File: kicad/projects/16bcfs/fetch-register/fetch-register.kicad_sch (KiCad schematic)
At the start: 104 parts, among them J1 InstrRegInput, J2 ALU Bus B, J3 FetchBusInput, J4 Main Bus, J5 Control Signals, J6 Address Bus 2, J7 Power, U1 74HC574, U10 74HC574, U11 74HC574, U12 74HC541, U2 74HC574, U3 74HC574, U4 74HC574, U5 74HC574, U6 74HC574, U7 74HC04, U8 74HC574, U9 74HC574

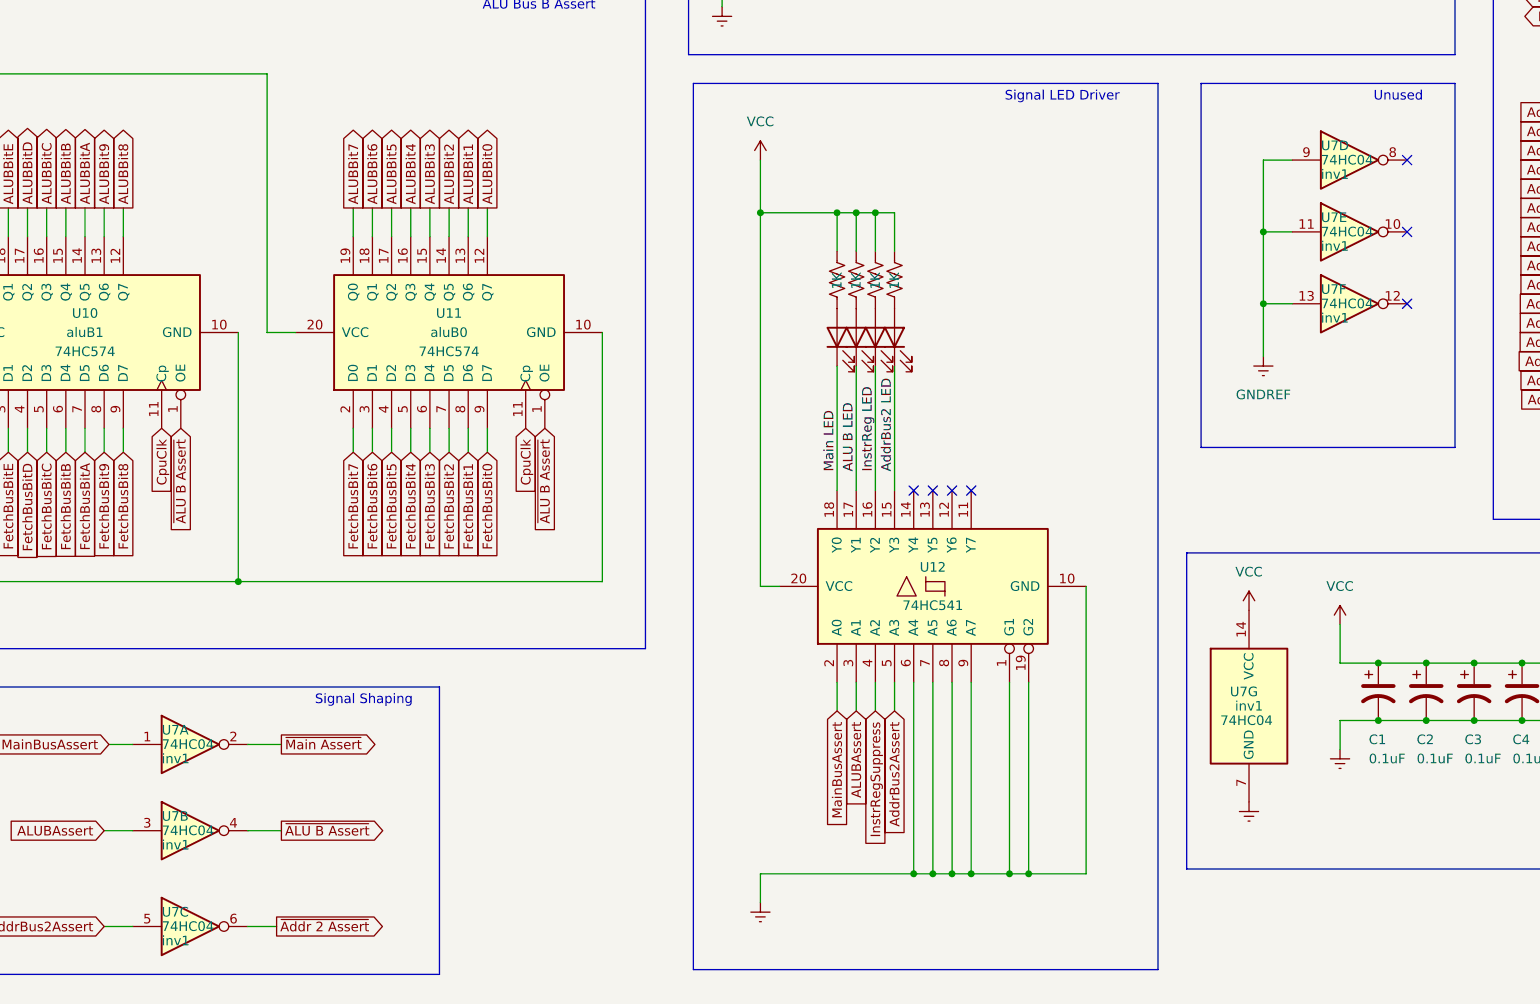
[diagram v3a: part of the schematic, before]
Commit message: Complete Component Placement on the Fetch Reg PCB
This commit handles all the component placement on the PCB for the Fetch
Register ahead of routing traces.  The expectation is that there is
plenty of room for traces.

Nothing has been done for 0R Resistors or test points yet.  Those will
be added ahead of routing.
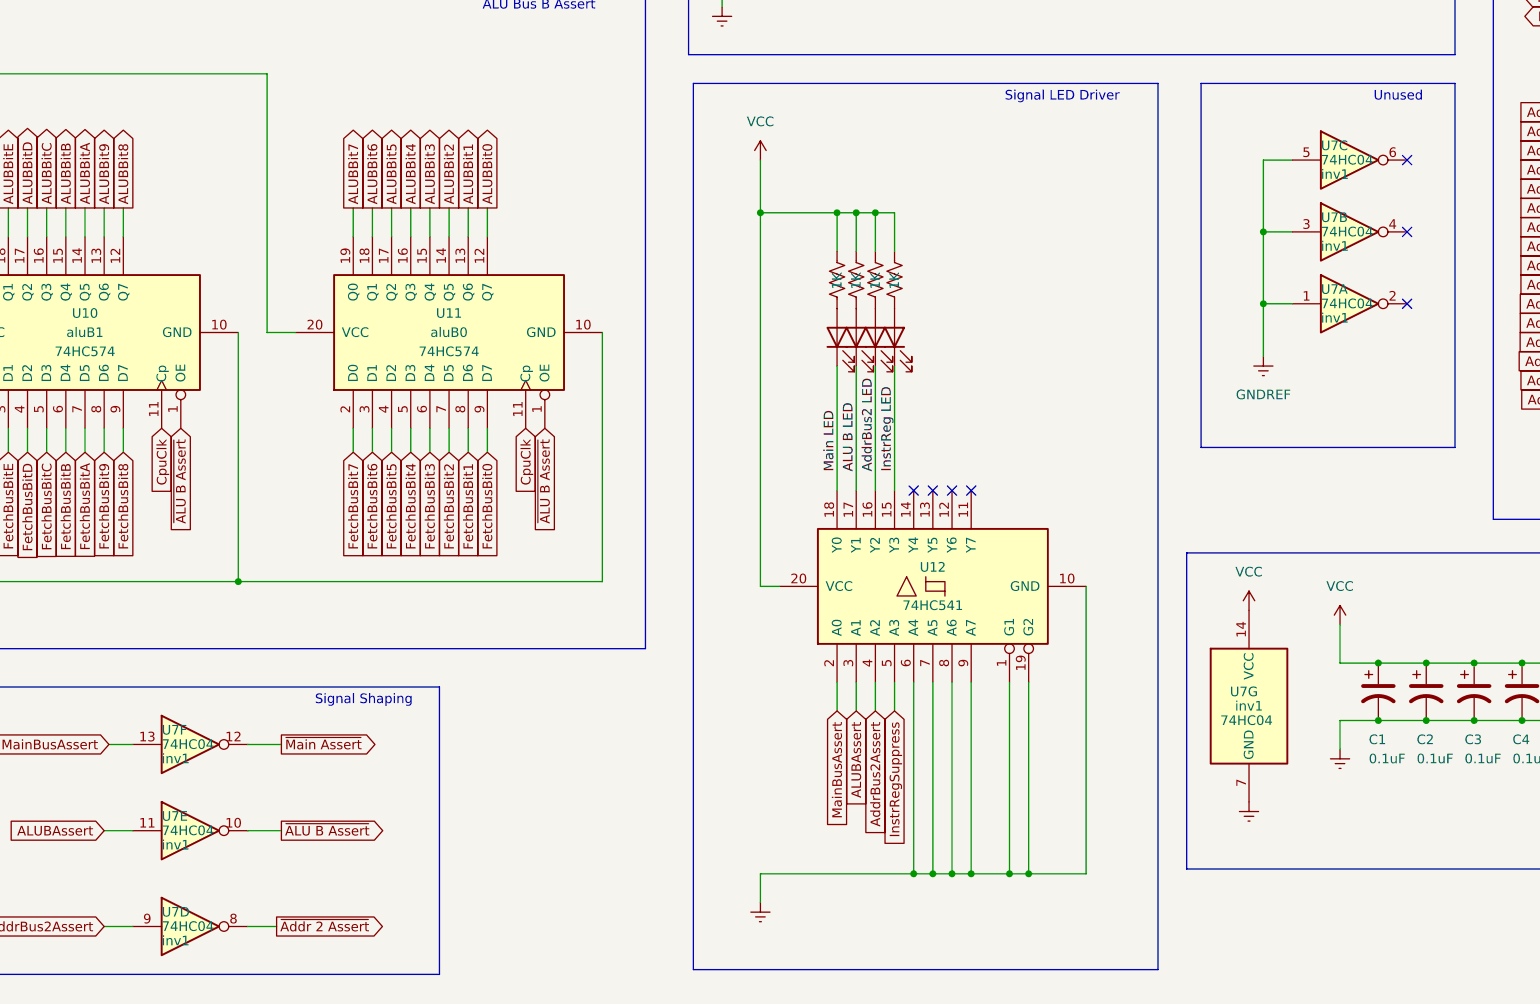
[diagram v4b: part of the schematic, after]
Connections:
- net ALUBAssert: now also U7.11; no longer U7.3
- net AddrBus2 LED: now also D19.1 (K), U12.16 (Y2); no longer D20.1 (K), U12.15 (Y3)
- net AddrBus2Assert: now also U12.4 (A2), U7.9; no longer U12.5 (A3), U7.5
- net GNDREF: now also U7.1, U7.3, U7.5; no longer U7.11, U7.13, U7.9
- net InstrReg LED: now also D20.1 (K), U12.15 (Y3); no longer D19.1 (K), U12.16 (Y2)
- net InstrRegSuppress: now also U12.5 (A3); no longer U12.4 (A2)
- net MainBusAssert: now also U7.13; no longer U7.1
- net ~{ALU B Assert}: now also U7.10; no longer U7.4
- net ~{Addr 2 Assert}: now also U7.8; no longer U7.6
- net ~{Main Assert}: now also U7.12; no longer U7.2
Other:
- moved on the sheet: U7A, U7B, U7C, U7D, U7E, U7F
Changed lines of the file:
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@@
     (effects (font (size 1.27 1.27)) (justify left bottom))
   )
-  (label "AddrBus2 LED" (at 256.54 171.45 90) (fields_autoplaced)
+  (label "AddrBus2 LED" (at 254 171.45 90) (fields_autoplaced)
     (effects (font (size 1.27 1.27)) (justify left bottom))
   )
@@
     (effects (font (size 1.27 1.27)) (justify left bottom))
   )
-  (label "InstrReg LED" (at 254 171.45 90) (fields_autoplaced)
+  (label "InstrReg LED" (at 256.54 171.45 90) (fields_autoplaced)
     (effects (font (size 1.27 1.27)) (justify left bottom))
   )
@@
     )
   )
-  (global_label "InstrRegSuppress" (shape input) (at 254 203.2 270) (fields_autoplaced)
+  (global_label "InstrRegSuppress" (shape input) (at 256.54 203.2 270) (fields_autoplaced)
     (effects (font (size 1.27 1.27)) (justify right))
-    (property "Intersheetrefs" "${INTERSHEET_REFS}" (at 254 222.4947 90)
-      (effects (font (size 1.27 1.27)) (justify right) hide)
+    (property "Intersheetrefs" "${INTERSHEET_REFS}" (at 256.54 222.4947 90)
+      (effects (font (size 1.27 1.27)) (justify left) hide)
     )
   )
@@
     )
   )
-  (global_label "AddrBus2Assert" (shape input) (at 256.54 203.2 270) (fields_autoplaced)
+  (global_label "AddrBus2Assert" (shape input) (at 254 203.2 270) (fields_autoplaced)
     (effects (font (size 1.27 1.27)) (justify right))
-    (property "Intersheetrefs" "${INTERSHEET_REFS}" (at 256.54 220.6805 90)
-      (effects (font (size 1.27 1.27)) (justify right) hide)
+    (property "Intersheetrefs" "${INTERSHEET_REFS}" (at 254 220.6805 90)
+      (effects (font (size 1.27 1.27)) (justify left) hide)
     )
   )
@@
     )
   )
-  (symbol (lib_id "74xx:74HC04") (at 316.865 130.175 0) (unit 4)
+  (symbol (lib_id "74xx:74HC04") (at 163.195 231.775 0) (unit 4)
     (in_bom yes) (on_board yes) (dnp no)
-    (property "Reference" "U7" (at 313.055 128.27 0)
+    (property "Reference" "U7" (at 159.385 229.87 0)
       (effects (font (size 1.27 1.27)) (justify left))
     )
-    (property "Value" "74HC04" (at 313.055 130.175 0)
+    (property "Value" "74HC04" (at 159.385 231.775 0)
       (effects (font (size 1.27 1.27)) (justify left))
     )
-    (property "Footprint" "Package_SO:SOIC-14_3.9x8.7mm_P1.27mm" (at 316.865 130.175 0)
+    (property "Footprint" "Package_SO:SOIC-14_3.9x8.7mm_P1.27mm" (at 163.195 231.775 0)
       (effects (font (size 1.27 1.27)) hide)
     )
-    (property "Datasheet" "https://assets.nexperia.com/documents/data-sheet/74HC_HCT04.pdf" (at 316.865 130.175 0)
+    (property "Datasheet" "https://assets.nexperia.com/documents/data-sheet/74HC_HCT04.pdf" (at 163.195 231.775 0)
       (effects (font (size 1.27 1.27)) hide)
     )
-    (property "VarName" "inv1" (at 313.055 132.08 0)
+    (property "VarName" "inv1" (at 159.385 233.68 0)
       (effects (font (size 1.27 1.27)) (justify left))
     )
@@
     )
   )
-  (symbol (lib_id "74xx:74HC04") (at 316.865 149.225 0) (unit 6)
+  (symbol (lib_id "74xx:74HC04") (at 163.195 207.645 0) (unit 6)
     (in_bom yes) (on_board yes) (dnp no)
-    (property "Reference" "U7" (at 313.055 147.32 0)
+    (property "Reference" "U7" (at 159.385 205.74 0)
       (effects (font (size 1.27 1.27)) (justify left))
     )
-    (property "Value" "74HC04" (at 313.055 149.225 0)
+    (property "Value" "74HC04" (at 159.385 207.645 0)
       (effects (font (size 1.27 1.27)) (justify left))
     )
-    (property "Footprint" "Package_SO:SOIC-14_3.9x8.7mm_P1.27mm" (at 316.865 149.225 0)
+    (property "Footprint" "Package_SO:SOIC-14_3.9x8.7mm_P1.27mm" (at 163.195 207.645 0)
       (effects (font (size 1.27 1.27)) hide)
     )
-    (property "Datasheet" "https://assets.nexperia.com/documents/data-sheet/74HC_HCT04.pdf" (at 316.865 149.225 0)
+    (property "Datasheet" "https://assets.nexperia.com/documents/data-sheet/74HC_HCT04.pdf" (at 163.195 207.645 0)
       (effects (font (size 1.27 1.27)) hide)
     )
-    (property "VarName" "inv1" (at 313.055 151.13 0)
+    (property "VarName" "inv1" (at 159.385 209.55 0)
       (effects (font (size 1.27 1.27)) (justify left))
     )
@@
     )
   )
-  (symbol (lib_id "74xx:74HC04") (at 163.195 207.645 0) (unit 1)
+  (symbol (lib_id "74xx:74HC04") (at 316.865 149.225 0) (unit 1)
     (in_bom yes) (on_board yes) (dnp no)
-    (property "Reference" "U7" (at 159.385 205.74 0)
+    (property "Reference" "U7" (at 313.055 147.32 0)
       (effects (font (size 1.27 1.27)) (justify left))
     )
-    (property "Value" "74HC04" (at 159.385 207.645 0)
+    (property "Value" "74HC04" (at 313.055 149.225 0)
       (effects (font (size 1.27 1.27)) (justify left))
     )
-    (property "Footprint" "Package_SO:SOIC-14_3.9x8.7mm_P1.27mm" (at 163.195 207.645 0)
+    (property "Footprint" "Package_SO:SOIC-14_3.9x8.7mm_P1.27mm" (at 316.865 149.225 0)
       (effects (font (size 1.27 1.27)) hide)
     )
-    (property "Datasheet" "https://assets.nexperia.com/documents/data-sheet/74HC_HCT04.pdf" (at 163.195 207.645 0)
+    (property "Datasheet" "https://assets.nexperia.com/documents/data-sheet/74HC_HCT04.pdf" (at 316.865 149.225 0)
       (effects (font (size 1.27 1.27)) hide)
     )
-    (property "VarName" "inv1" (at 159.385 209.55 0)
+    (property "VarName" "inv1" (at 313.055 151.13 0)
       (effects (font (size 1.27 1.27)) (justify left))
     )
@@
     )
   )
-  (symbol (lib_id "74xx:74HC04") (at 163.195 231.775 0) (unit 3)
+  (symbol (lib_id "74xx:74HC04") (at 316.865 130.175 0) (unit 3)
     (in_bom yes) (on_board yes) (dnp no)
-    (property "Reference" "U7" (at 159.385 229.87 0)
+    (property "Reference" "U7" (at 313.055 128.27 0)
       (effects (font (size 1.27 1.27)) (justify left))
     )
-    (property "Value" "74HC04" (at 159.385 231.775 0)
+    (property "Value" "74HC04" (at 313.055 130.175 0)
       (effects (font (size 1.27 1.27)) (justify left))
     )
-    (property "Footprint" "Package_SO:SOIC-14_3.9x8.7mm_P1.27mm" (at 163.195 231.775 0)
+    (property "Footprint" "Package_SO:SOIC-14_3.9x8.7mm_P1.27mm" (at 316.865 130.175 0)
       (effects (font (size 1.27 1.27)) hide)
     )
-    (property "Datasheet" "https://assets.nexperia.com/documents/data-sheet/74HC_HCT04.pdf" (at 163.195 231.775 0)
+    (property "Datasheet" "https://assets.nexperia.com/documents/data-sheet/74HC_HCT04.pdf" (at 316.865 130.175 0)
       (effects (font (size 1.27 1.27)) hide)
     )
-    (property "VarName" "inv1" (at 159.385 233.68 0)
+    (property "VarName" "inv1" (at 313.055 132.08 0)
       (effects (font (size 1.27 1.27)) (justify left))
     )
@@
     )
   )
-  (symbol (lib_id "74xx:74HC04") (at 163.195 219.075 0) (unit 2)
+  (symbol (lib_id "74xx:74HC04") (at 316.865 139.7 0) (unit 2)
     (in_bom yes) (on_board yes) (dnp no)
-    (property "Reference" "U7" (at 159.385 217.17 0)
+    (property "Reference" "U7" (at 313.055 137.795 0)
       (effects (font (size 1.27 1.27)) (justify left))
     )
-    (property "Value" "74HC04" (at 159.385 219.075 0)
+    (property "Value" "74HC04" (at 313.055 139.7 0)
       (effects (font (size 1.27 1.27)) (justify left))
     )
-    (property "Footprint" "Package_SO:SOIC-14_3.9x8.7mm_P1.27mm" (at 163.195 219.075 0)
+    (property "Footprint" "Package_SO:SOIC-14_3.9x8.7mm_P1.27mm" (at 316.865 139.7 0)
       (effects (font (size 1.27 1.27)) hide)
     )
-    (property "Datasheet" "https://assets.nexperia.com/documents/data-sheet/74HC_HCT04.pdf" (at 163.195 219.075 0)
+    (property "Datasheet" "https://assets.nexperia.com/documents/data-sheet/74HC_HCT04.pdf" (at 316.865 139.7 0)
       (effects (font (size 1.27 1.27)) hide)
     )
-    (property "VarName" "inv1" (at 159.385 220.98 0)
+    (property "VarName" "inv1" (at 313.055 141.605 0)
       (effects (font (size 1.27 1.27)) (justify left))
     )
@@
     )
   )
-  (symbol (lib_id "74xx:74HC04") (at 316.865 139.7 0) (unit 5)
+  (symbol (lib_id "74xx:74HC04") (at 163.195 219.075 0) (unit 5)
     (in_bom yes) (on_board yes) (dnp no)
-    (property "Reference" "U7" (at 313.055 137.795 0)
+    (property "Reference" "U7" (at 159.385 217.17 0)
       (effects (font (size 1.27 1.27)) (justify left))
     )
-    (property "Value" "74HC04" (at 313.055 139.7 0)
+    (property "Value" "74HC04" (at 159.385 219.075 0)
       (effects (font (size 1.27 1.27)) (justify left))
     )
-    (property "Footprint" "Package_SO:SOIC-14_3.9x8.7mm_P1.27mm" (at 316.865 139.7 0)
+    (property "Footprint" "Package_SO:SOIC-14_3.9x8.7mm_P1.27mm" (at 163.195 219.075 0)
       (effects (font (size 1.27 1.27)) hide)
     )
-    (property "Datasheet" "https://assets.nexperia.com/documents/data-sheet/74HC_HCT04.pdf" (at 316.865 139.7 0)
+    (property "Datasheet" "https://assets.nexperia.com/documents/data-sheet/74HC_HCT04.pdf" (at 163.195 219.075 0)
       (effects (font (size 1.27 1.27)) hide)
     )
-    (property "VarName" "inv1" (at 313.055 141.605 0)
+    (property "VarName" "inv1" (at 159.385 220.98 0)
       (effects (font (size 1.27 1.27)) (justify left))
     )

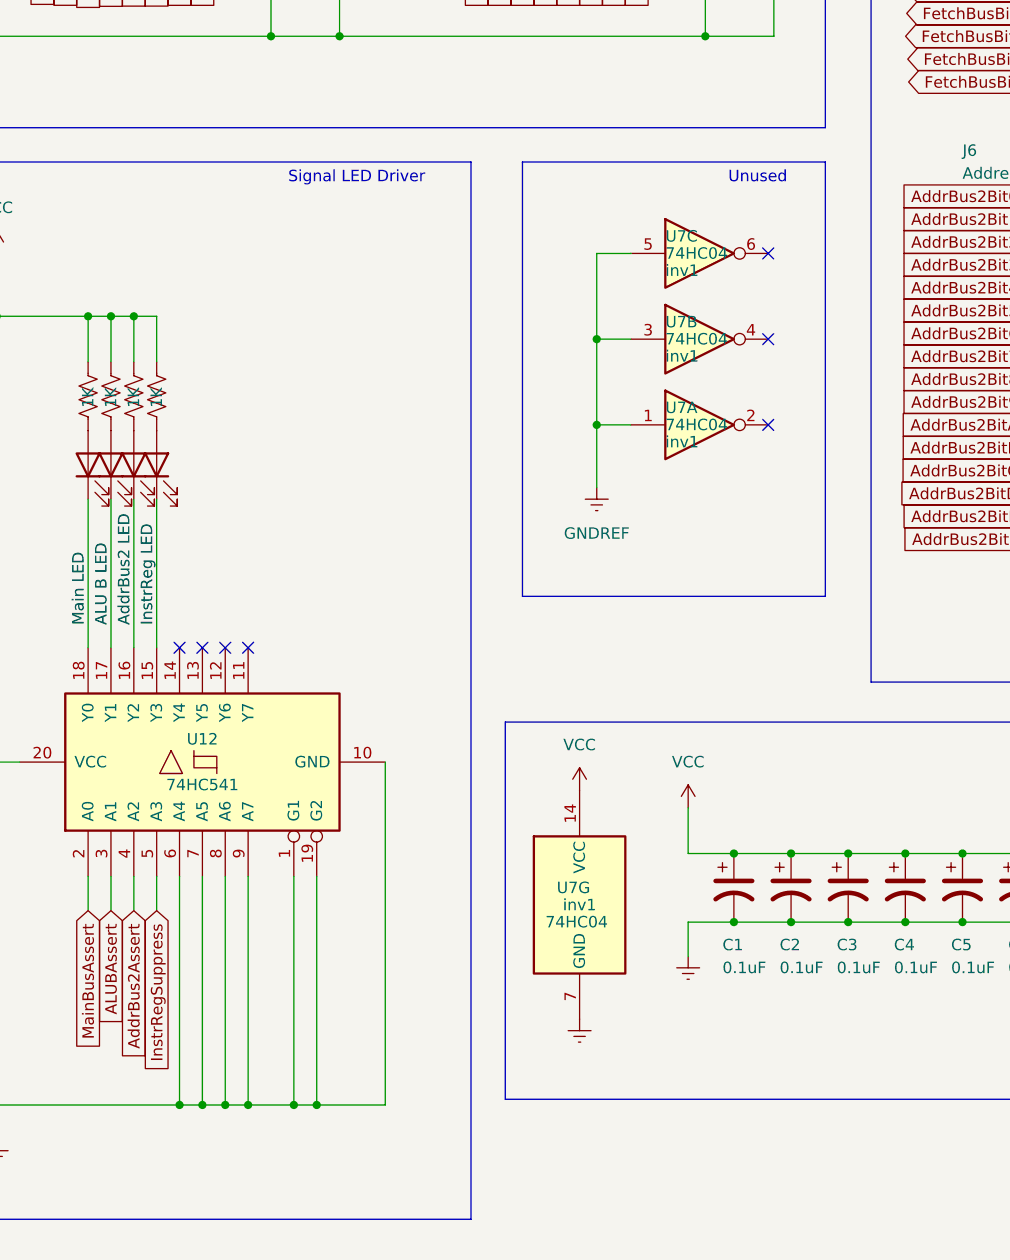
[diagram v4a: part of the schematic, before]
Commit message: Add 0R Resistors and Test Points to the PCB
Get this done before routing the PCB
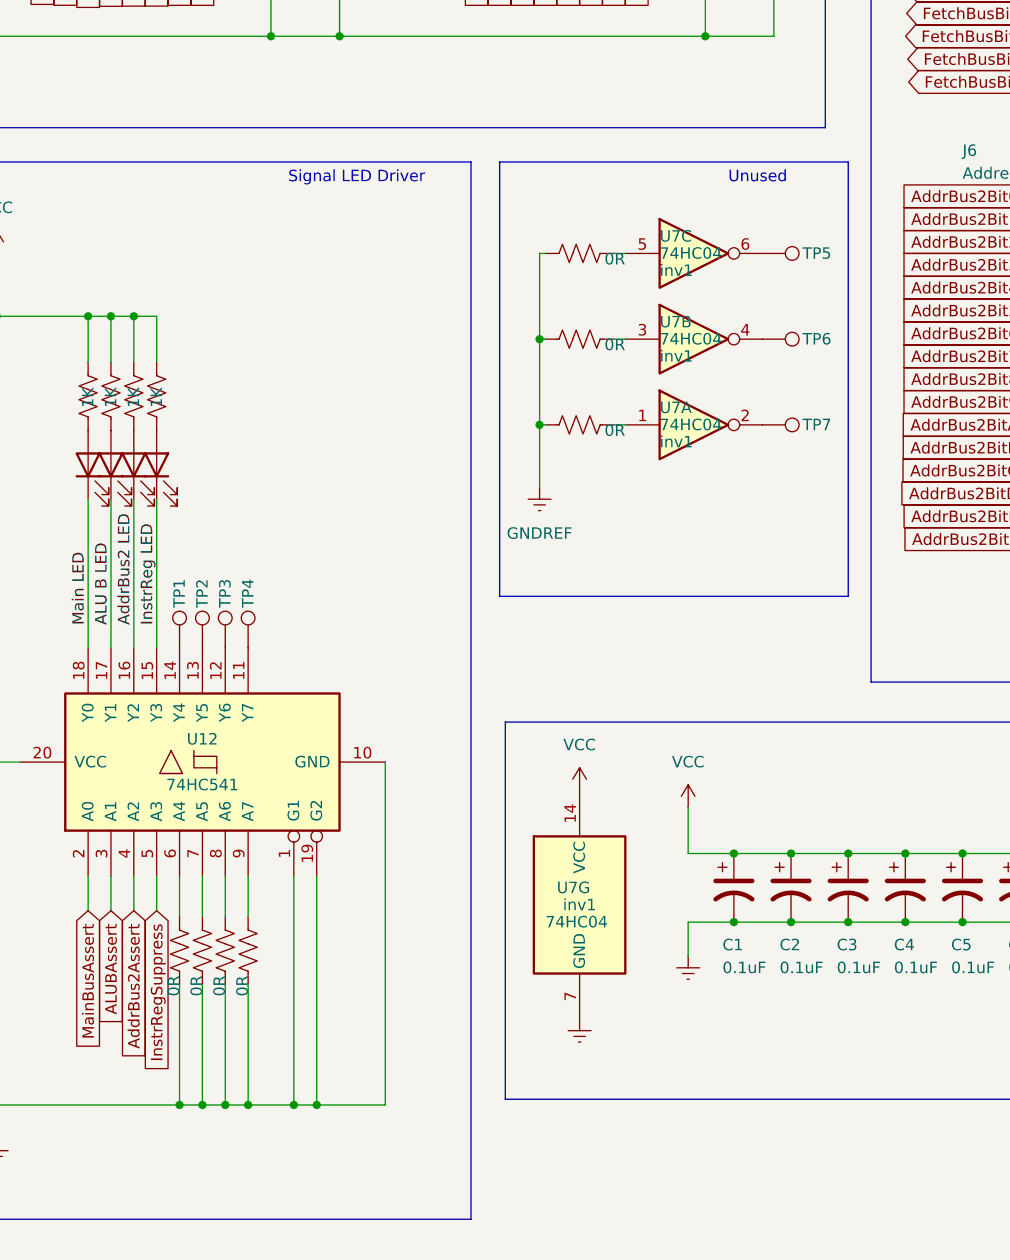
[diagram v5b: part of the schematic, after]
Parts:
- added R53, R54, R55, R56, R57, R58, R59: 0R, Resistor_SMD:R_1206_3216Metric_Pad1.30x1.75mm_HandSolder, symbol Device:R_US
- added TP1, TP2, TP3, TP4, TP5, TP6, TP7: TestPoint, eryjus:TestPoint_SMD_D0.8mm, symbol Connector:TestPoint
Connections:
- net GNDREF: now also R53.2, R54.2, R55.2, R56.2, R57.1, R58.1, R59.1; no longer U12.6 (A4), U12.7 (A5), U12.8 (A6), U12.9 (A7), U7.1, U7.3, U7.5
- net at U7.2: now also TP7.1
- net at U7.6: now also TP5.1
- net at U7.4: now also TP6.1
- net at U12.11 (Y7): now also TP4.1
- net at U12.12 (Y6): now also TP3.1
- net at U12.13 (Y5): now also TP2.1
- net at U12.14 (Y4): now also TP1.1
- new net: R56.1, U12.9 (A7)
- new net: R53.1, U12.6 (A4)
- new net: R59.2, U7.5
- new net: R57.2, U7.1
- new net: R58.2, U7.3
- new net: R54.1, U12.7 (A5)
- new net: R55.1, U12.8 (A6)
- no-connect marks 9 -> 2
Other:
- moved on the sheet: U7A, U7B, U7C
